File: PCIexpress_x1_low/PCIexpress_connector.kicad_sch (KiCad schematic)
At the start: 2 parts, among them J1 PCIexpress_bracket, J2 PCIexpress_x1

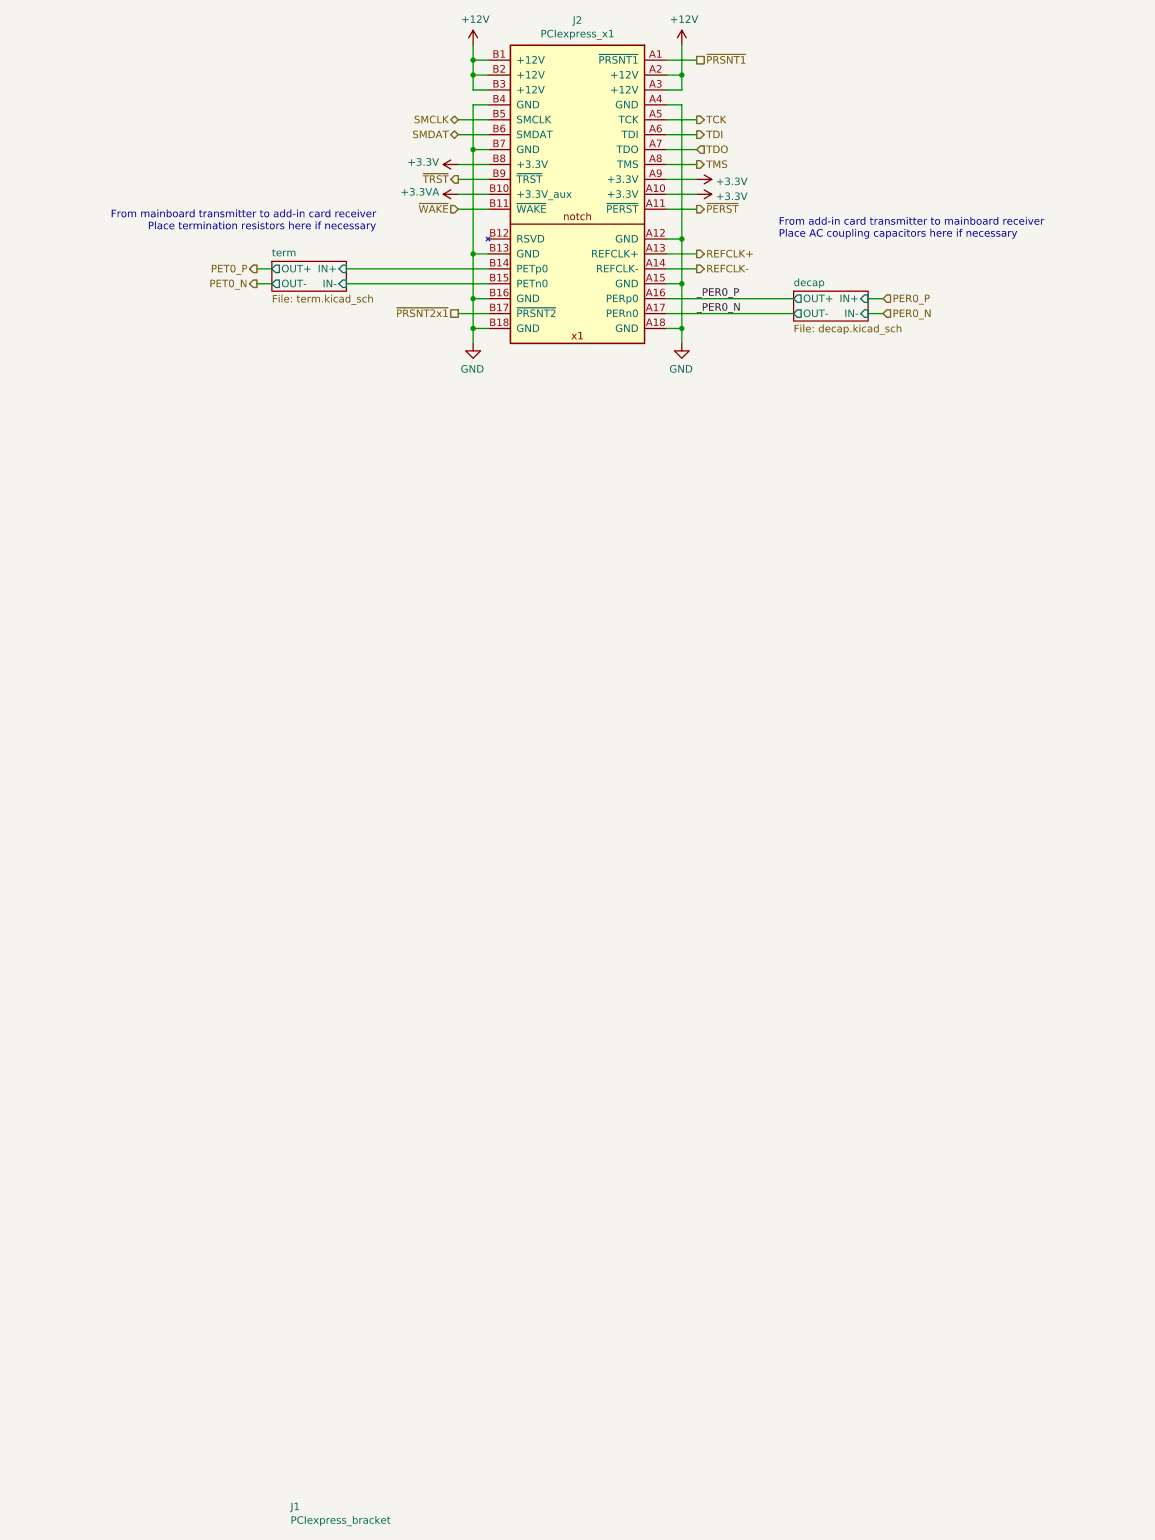
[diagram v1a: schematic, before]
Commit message: working to route 0.8mm pitch bga, probably not practical
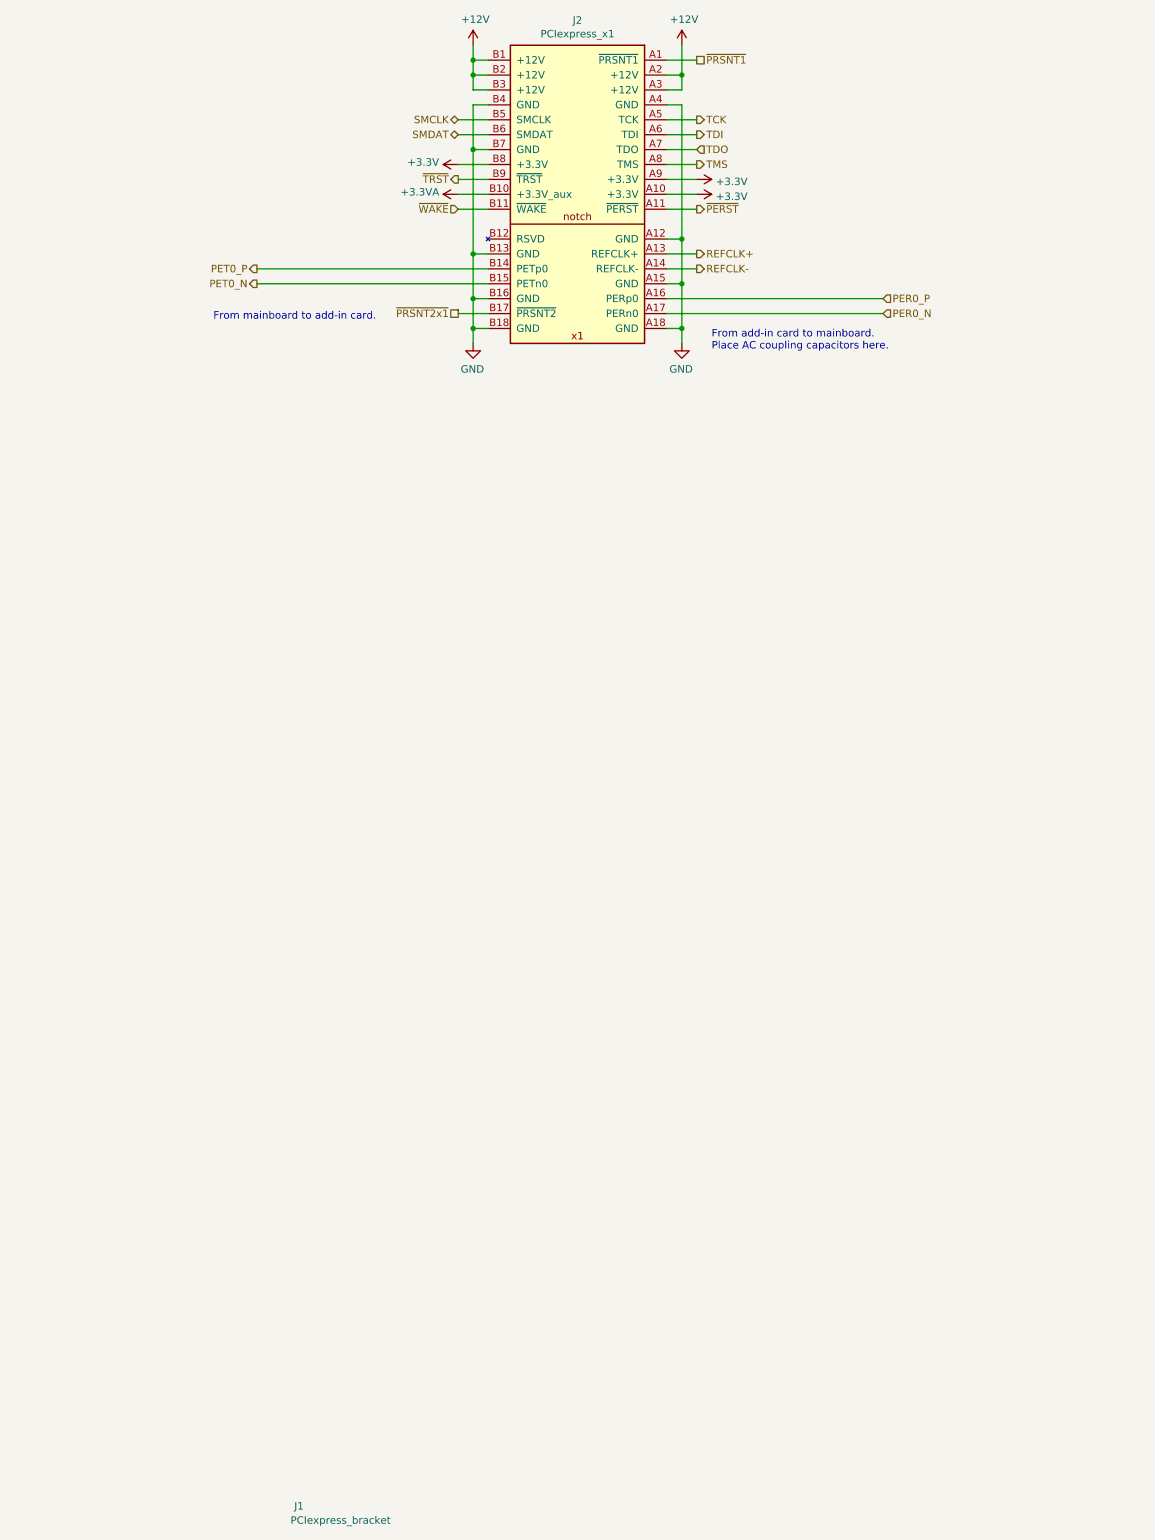
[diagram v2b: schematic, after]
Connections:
- net _PER0_N is gone; now on net PER0_N: J2.A17 (PERn0)
- net _PER0_P is gone; now on net PER0_P: J2.A16 (PERp0)
- net term/IN+ is gone; now on net PET0_P: J2.B14 (PETp0)
- net term/IN- is gone; now on net PET0_N: J2.B15 (PETn0)
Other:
- removed sheet decap
- removed sheet term
- note added: "From add-in card to mainboard. Place AC coupling capacitors here."
- note added: "From mainboard to add-in card."
- note removed: "From add-in card transmitter to mainboard receiver Place AC coupling capacitors here if necessary"
- note removed: "From mainboard transmitter to add-in card receiver Place termination resistors here if necessary"
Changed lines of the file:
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@@
-    (stroke (width 0) (type default))
-  )
-  (wire (pts (xy 50.8 63.5) (xy 53.34 63.5))
-    (stroke (width 0) (type default))
-  )
-  (wire (pts (xy 154.94 68.58) (xy 157.48 68.58))
     (stroke (width 0) (type default))
   )
@@
     (stroke (width 0) (type default))
   )
-  (wire (pts (xy 154.94 66.04) (xy 157.48 66.04))
-    (stroke (width 0) (type default))
-  )
   (wire (pts (xy 120.65 48.26) (xy 125.73 48.26))
     (stroke (width 0) (type default))
@@
     (stroke (width 0) (type default))
   )
-  (wire (pts (xy 120.65 66.04) (xy 142.24 66.04))
+  (wire (pts (xy 120.65 66.04) (xy 157.48 66.04))
     (stroke (width 0) (type default))
   )
@@
     (stroke (width 0) (type default))
   )
-  (wire (pts (xy 66.04 63.5) (xy 90.17 63.5))
+  (wire (pts (xy 50.8 63.5) (xy 90.17 63.5))
     (stroke (width 0) (type default))
   )
@@
     (stroke (width 0) (type default))
   )
-  (wire (pts (xy 66.04 60.96) (xy 90.17 60.96))
+  (wire (pts (xy 50.8 60.96) (xy 90.17 60.96))
     (stroke (width 0) (type default))
   )
@@
     (stroke (width 0) (type default))
   )
-  (wire (pts (xy 120.65 68.58) (xy 142.24 68.58))
-    (stroke (width 0) (type default))
-  )
-  (wire (pts (xy 50.8 60.96) (xy 53.34 60.96))
+  (wire (pts (xy 120.65 68.58) (xy 157.48 68.58))
     (stroke (width 0) (type default))
   )
@@
     (stroke (width 0) (type default))
   )
-  (text "From mainboard transmitter to add-in card receiver\nPlace termination resistors here if necessary"
-    (at 71.12 54.61 0)
+  (text "From mainboard to add-in card." (at 71.12 69.85 0)
     (effects (font (size 1.27 1.27)) (justify right bottom))
   )
-  (text "From add-in card transmitter to mainboard receiver\nPlace AC coupling capacitors here if necessary"
-    (at 139.7 55.88 0)
-    (effects (font (size 1.27 1.27)) (justify left bottom))
-  )
-  (label "_PER0_P" (at 125.73 66.04 0) (fields_autoplaced)
-    (effects (font (size 1.27 1.27)) (justify left bottom))
-  )
-  (label "_PER0_N" (at 125.73 68.58 0) (fields_autoplaced)
+  (text "From add-in card to mainboard.\nPlace AC coupling capacitors here."
+    (at 128.27 74.93 0)
     (effects (font (size 1.27 1.27)) (justify left bottom))
   )
@@
   (symbol (lib_id "PCIexpress:PCIexpress_bracket") (at 55.88 273.05 0) (unit 1)
     (in_bom yes) (on_board yes) (dnp no)
-    (property "Reference" "J1" (at 56.515 271.8816 0)
+    (property "Reference" "J1" (at 57.15 271.78 0)
       (effects (font (size 1.27 1.27)) (justify left))
     )
@@
       )
     )
-  )
-  (sheet (at 53.34 59.69) (size 12.7 5.08) (fields_autoplaced)
-    (stroke (width 0) (type solid))
-    (fill (color 0 0 0 0.0000))
-    (property "Sheetname" "term" (at 53.34 58.9784 0)
-      (effects (font (size 1.27 1.27)) (justify left bottom))
-    )
-    (property "Sheetfile" "term.kicad_sch" (at 53.34 65.3546 0)
-      (effects (font (size 1.27 1.27)) (justify left top))
-    )
-    (pin "IN+" input (at 66.04 60.96 0)
-      (effects (font (size 1.27 1.27)) (justify right))
-    )
-    (pin "IN-" input (at 66.04 63.5 0)
-      (effects (font (size 1.27 1.27)) (justify right))
-    )
-    (pin "OUT+" output (at 53.34 60.96 180)
-      (effects (font (size 1.27 1.27)) (justify left))
-    )
-    (pin "OUT-" output (at 53.34 63.5 180)
-      (effects (font (size 1.27 1.27)) (justify left))
-    )
-    (instances
-      (project "PCIexpress_x1_low"
-        (path "/b58173cd-28d5-49a4-a789-299fbf6f5cc2/00000000-0000-0000-0000-00005d508b15" (page "3"))
-      )
-    )
-  )
-  (sheet (at 142.24 64.77) (size 12.7 5.08) (fields_autoplaced)
-    (stroke (width 0) (type solid))
-    (fill (color 0 0 0 0.0000))
-    (property "Sheetname" "decap" (at 142.24 64.0584 0)
-      (effects (font (size 1.27 1.27)) (justify left bottom))
-    )
-    (property "Sheetfile" "decap.kicad_sch" (at 142.24 70.4346 0)
-      (effects (font (size 1.27 1.27)) (justify left top))
-    )
-    (pin "IN+" input (at 154.94 66.04 0)
-      (effects (font (size 1.27 1.27)) (justify right))
-    )
-    (pin "OUT+" output (at 142.24 66.04 180)
-      (effects (font (size 1.27 1.27)) (justify left))
-    )
-    (pin "OUT-" output (at 142.24 68.58 180)
-      (effects (font (size 1.27 1.27)) (justify left))
-    )
-    (pin "IN-" input (at 154.94 68.58 0)
-      (effects (font (size 1.27 1.27)) (justify right))
-    )
-    (instances
-      (project "PCIexpress_x1_low"
-        (path "/b58173cd-28d5-49a4-a789-299fbf6f5cc2/00000000-0000-0000-0000-00005d508b15" (page "4"))
-      )
-    )

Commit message: threw down some LEDs
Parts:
- removed J1: PCIexpress_bracket, PCIexpress:PCIexpress_bracket_low, symbol PCIexpress:PCIexpress_bracket
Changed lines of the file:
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@@
-    )
-  )
-  (symbol (lib_id "PCIexpress:PCIexpress_bracket") (at 55.88 273.05 0) (unit 1)
-    (in_bom yes) (on_board yes) (dnp no)
-    (property "Reference" "J1" (at 57.15 271.78 0)
-      (effects (font (size 1.27 1.27)) (justify left))
-    )
-    (property "Value" "PCIexpress_bracket" (at 56.515 274.193 0)
-      (effects (font (size 1.27 1.27)) (justify left))
-    )
-    (property "Footprint" "PCIexpress:PCIexpress_bracket_low" (at 55.88 273.05 0)
-      (effects (font (size 1.27 1.27)) hide)
-    )
-    (property "Datasheet" "" (at 55.88 273.05 0)
-      (effects (font (size 1.27 1.27)) hide)
-    )
-    (instances
-      (project "PCIexpress_x1_low"
-        (path "/b58173cd-28d5-49a4-a789-299fbf6f5cc2/00000000-0000-0000-0000-00005d508b15"
-          (reference "J1") (unit 1)
-        )
-      )
     )
   )

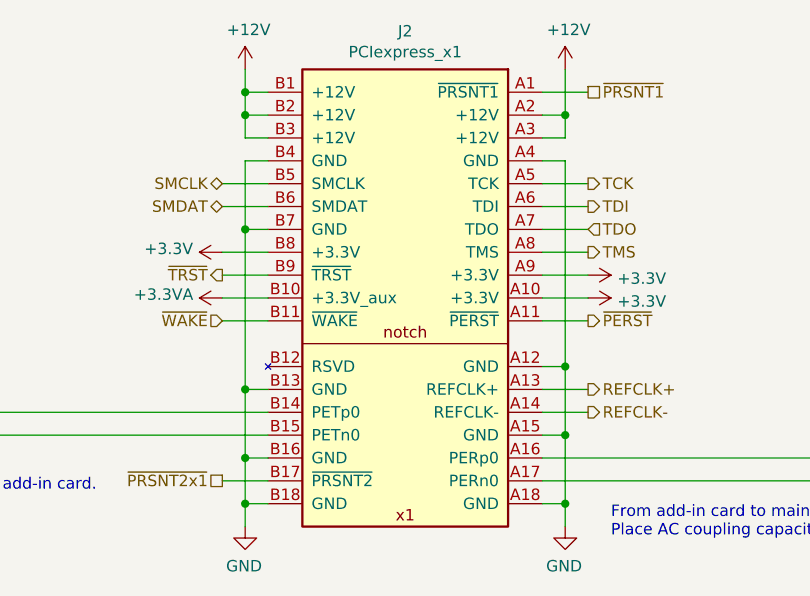
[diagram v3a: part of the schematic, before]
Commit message: adding AC coupling caps
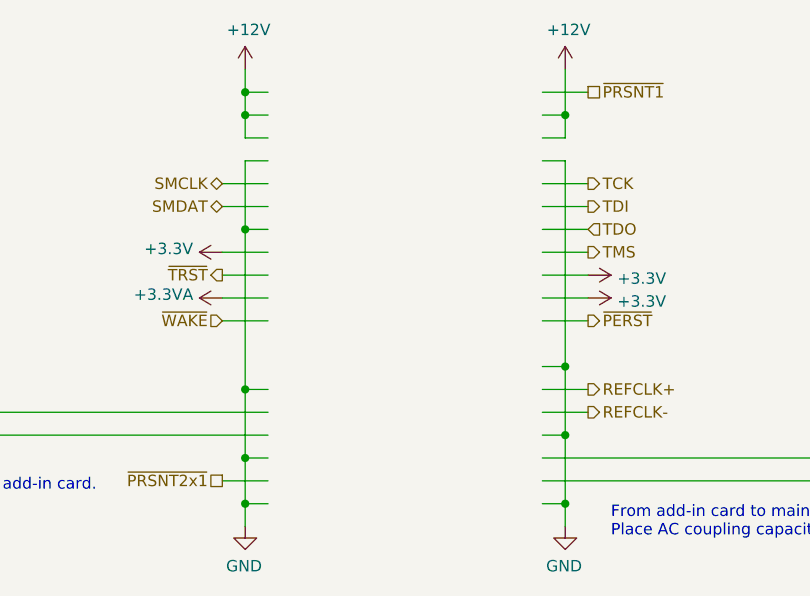
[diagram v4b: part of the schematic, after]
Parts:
- removed J2: PCIexpress_x1, PCIexpress:PCIexpress_x1, symbol PCIexpress:PCIexpress_x1
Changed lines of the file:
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@@
     (effects (font (size 1.27 1.27)) (justify left))
-  )
-  (symbol (lib_id "PCIexpress:PCIexpress_x1") (at 105.41 22.86 0) (unit 1)
-    (in_bom yes) (on_board yes) (dnp no)
-    (property "Reference" "J2" (at 105.41 18.6182 0)
-      (effects (font (size 1.27 1.27)))
-    )
-    (property "Value" "PCIexpress_x1" (at 105.41 20.9296 0)
-      (effects (font (size 1.27 1.27)))
-    )
-    (property "Footprint" "PCIexpress:PCIexpress_x1" (at 105.41 46.99 0)
-      (effects (font (size 1.27 1.27)) hide)
-    )
-    (property "Datasheet" "" (at 105.41 46.99 0)
-      (effects (font (size 1.27 1.27)) hide)
-    )
-    (pin "A1")
-    (pin "A10")
-    (pin "A11")
-    (pin "A12")
-    (pin "A13")
-    (pin "A14")
-    (pin "A15")
-    (pin "A16")
-    (pin "A17")
-    (pin "A18")
-    (pin "A2")
-    (pin "A3")
-    (pin "A4")
-    (pin "A5")
-    (pin "A6")
-    (pin "A7")
-    (pin "A8")
-    (pin "A9")
-    (pin "B1")
-    (pin "B10")
-    (pin "B11")
-    (pin "B12")
-    (pin "B13")
-    (pin "B14")
-    (pin "B15")
-    (pin "B16")
-    (pin "B17")
-    (pin "B18")
-    (pin "B2")
-    (pin "B3")
-    (pin "B4")
-    (pin "B5")
-    (pin "B6")
-    (pin "B7")
-    (pin "B8")
-    (pin "B9")
-    (instances
-      (project "PCIexpress_x1_low"
-        (path "/b58173cd-28d5-49a4-a789-299fbf6f5cc2/00000000-0000-0000-0000-00005d508b15"
-          (reference "J2") (unit 1)
-        )
-      )
-    )
   )
   (symbol (lib_id "power:GND") (at 87.63 73.66 0) (mirror y) (unit 1)
